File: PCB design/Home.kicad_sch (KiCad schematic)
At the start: 20 parts, among them J1 Fan, J2 LCD, J3 EM lock, J4 ACS712 Signal, J5 Power In, J7 RFID, J8 RFID, J9 LCD, K1 SANYOU_SRD_Form_C, U1 ACS712, U3 DHT11, U5 PIR, U6 MQ2

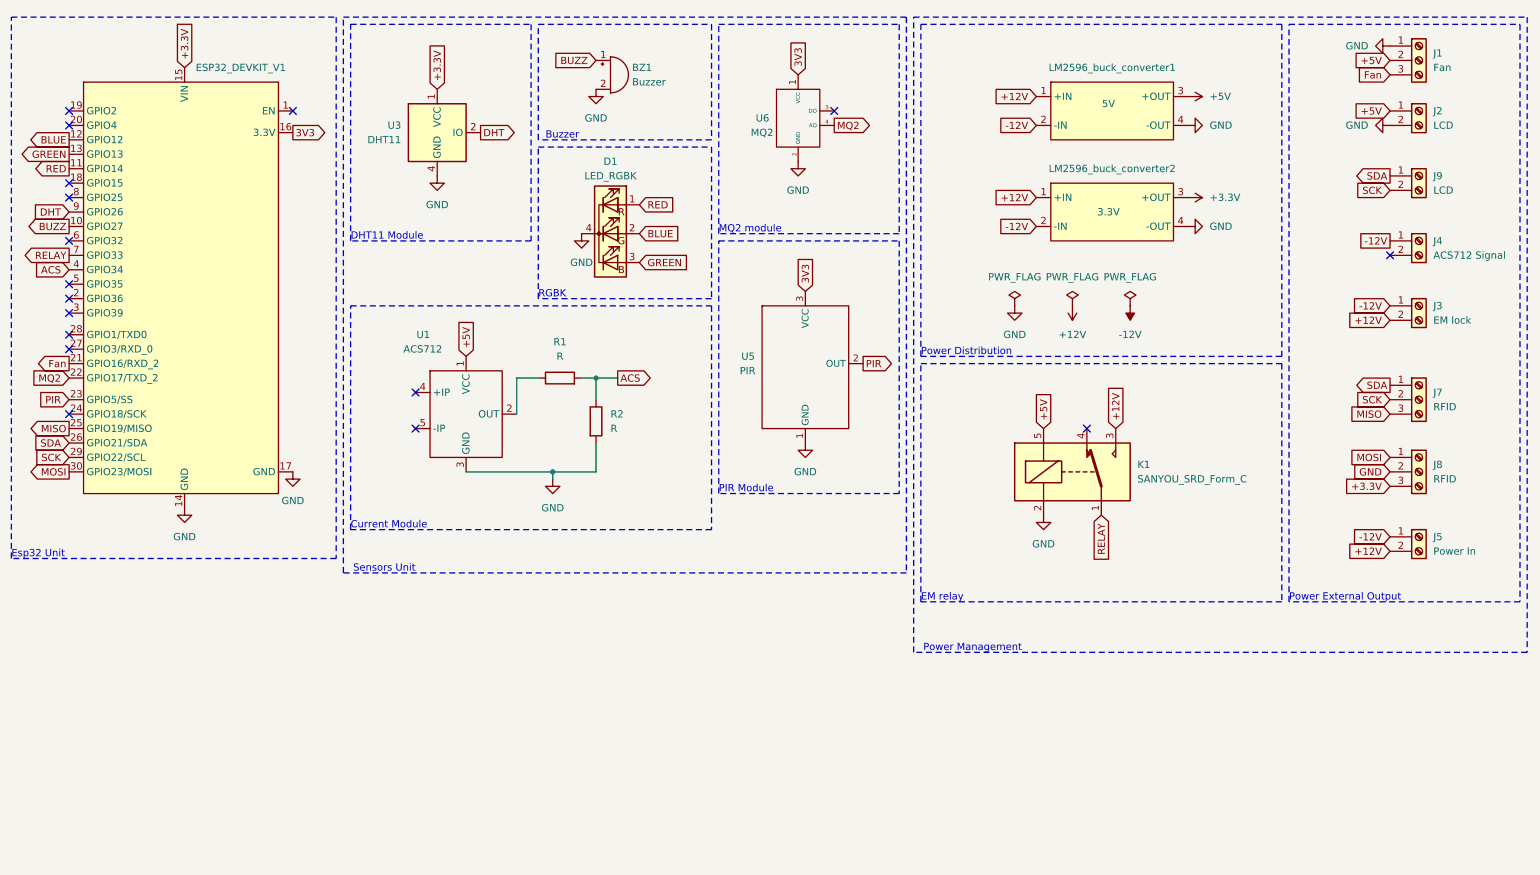
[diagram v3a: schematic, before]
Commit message: PCB with thicker tracks
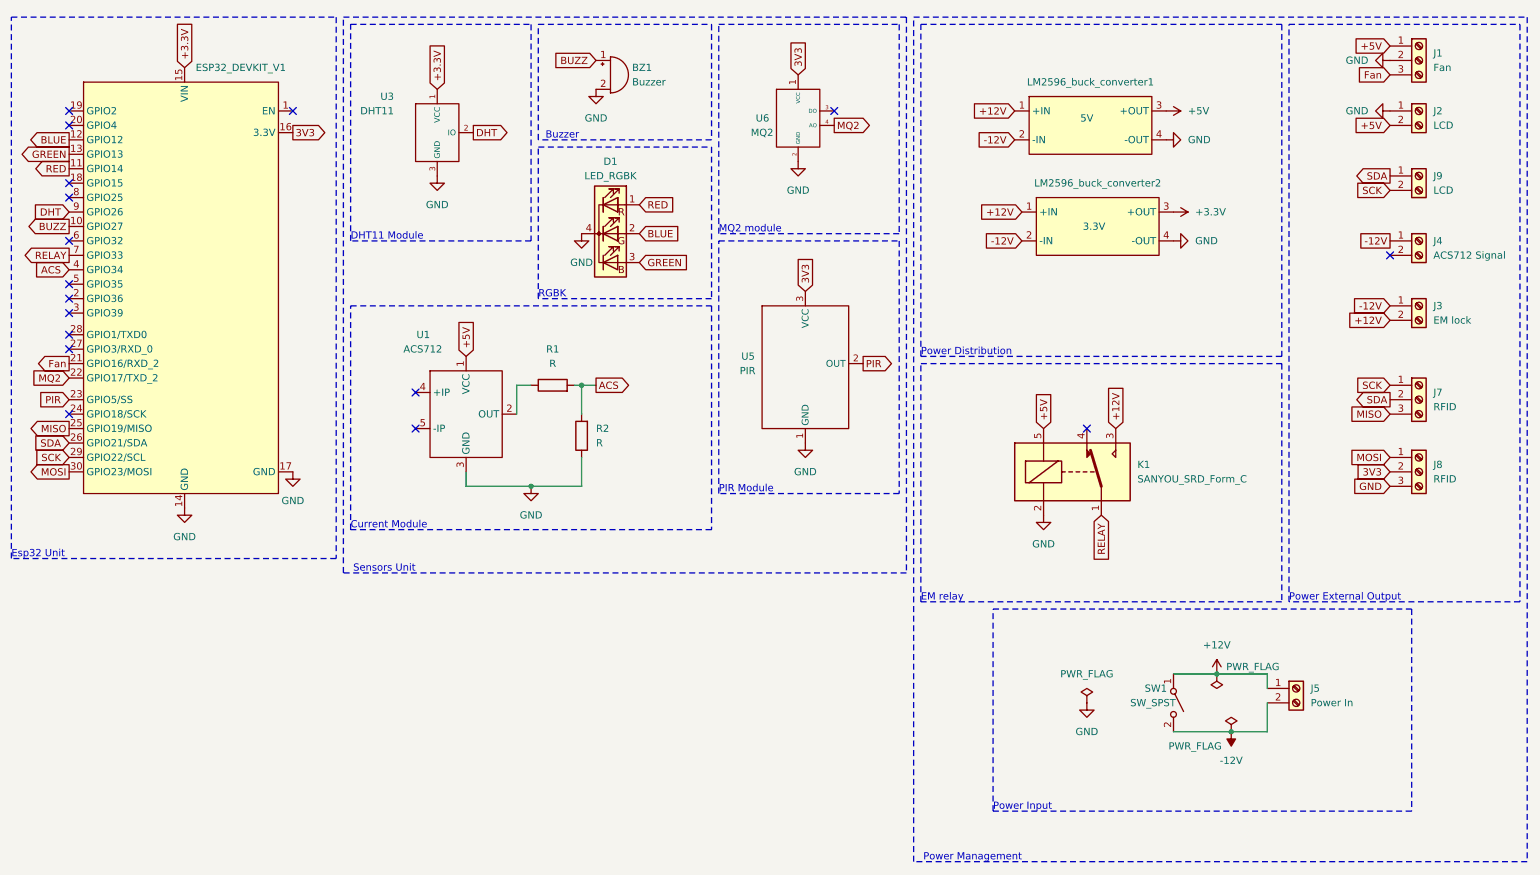
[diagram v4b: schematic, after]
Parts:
- added SW1: SW_SPST, Switch_SPST:SPST - KCD1-11, symbol Switch:SW_SPST
- D1: footprint LED_THT:LED_D5.0mm-4_RGB -> LED:RGB_LED
- U3: footprint Sensor:Aosong_DHT11_5.5x12.0_P2.54mm -> Sensor_temperature_humidity:DHT11_KY-015; symbol Sensor:DHT11 -> Sensor_temperature_and_humidity_DHT11_KY-015:DHT11_KY-015
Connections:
- net +12V: now also J5.1 (Pin_1), SW1.1 (A); no longer J5.2 (Pin_2)
- net +3.3V: no longer J8.3 (Pin_3)
- net +5V: now also J1.1 (Pin_1), J2.2 (Pin_2); no longer J1.2 (Pin_2), J2.1 (Pin_1)
- net -12V: now also J5.2 (Pin_2), SW1.2 (B); no longer J5.1 (Pin_1)
- net 3V3: now also J8.2 (Pin_2)
- net ACS: now also R2.2; no longer R2.1
- net GND: now also J1.2 (Pin_2), J2.1 (Pin_1), J8.3 (Pin_3), R2.1, U3.3 (GND); no longer J1.1 (Pin_1), J2.2 (Pin_2), J8.2 (Pin_2), R2.2, U3.4 (GND)
- net SCK: now also J7.1 (Pin_1); no longer J7.2 (Pin_2)
- net SDA: now also J7.2 (Pin_2); no longer J7.1 (Pin_1)
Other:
- note added: "Power Input"
- moved on the sheet: LM2596_buck_converter1, LM2596_buck_converter2
